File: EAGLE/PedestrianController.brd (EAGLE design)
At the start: 30 x 80 mm, 16 parts, among them CON1 FTDI, CON2 DS3231, CON3 AC110V, CON4 SIGNAL, IC1 ESP-WROOM-02

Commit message: Rearranged.
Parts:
- moved PROGSW 53.0 mm to (8.71, 79.7)
- moved R4 38.1 mm to (43.7, 53.8)
- moved RSTSW 36.0 mm to (8.71, 71.6)
- moved R5 35.0 mm to (43.7, 62.9)
- moved R6 35.0 mm to (43.7, 59.9)
- moved R7 35.0 mm to (43.7, 56.9)
- moved R1 27.8 mm to (43.7, 78.0)
- moved R2 27.8 mm to (43.7, 75.0)
- moved R3 27.8 mm to (43.7, 72.0)
- moved CON2 21.4 mm to (41.4, 46.1)
- moved CON1 14.0 mm to (8.55, 58.5), turned to 90 degrees
- moved SSR1 13.3 mm to (4.97, 27.3)
- moved CON4 11.7 mm to (34.8, 7.94)
- moved IC1 11.7 mm to (26.2, 77.7)
- moved SSR2 11.4 mm to (15.0, 27.3)
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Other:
- board size 30 x 80 mm -> 57.8 x 85 mm
- board text added: "Pedestrian Controller"
- board text added: "TAKACHI SW-100"
- board text added: "https://github.com/kekyo/PedestrianController"

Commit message: Rearranged parts.
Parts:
- moved R4 23.0 mm to (43.7, 76.8)
- moved R1 21.0 mm to (43.7, 57.0)
- moved R2 15.0 mm to (43.7, 60.0)
- moved R5 11.0 mm to (43.7, 73.9)
- moved R6 11.0 mm to (43.7, 70.9)
- moved R7 6.00 mm to (43.7, 62.9)
- moved R3 4.00 mm to (43.7, 68.0)
- moved CON3 2.00 mm to (13.8, 7.94)
- moved PROGSW 2.00 mm to (8.71, 77.7)
- moved RSTSW 2.00 mm to (8.71, 69.6)
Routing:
- net GND: track 0.00 -> 113.7 mm, vias 0 -> 1
- net +3V3: track 0.00 -> 101.6 mm
- net N$2: track 0.00 -> 58.6 mm, vias 0 -> 1
- net N$9: track 0.00 -> 58.4 mm
- net N$3: track 0.00 -> 51.9 mm
- net N$10: track 0.00 -> 50.1 mm
- net N$1: track 0.00 -> 45.9 mm
- net N$4: track 0.00 -> 41.5 mm
- net N$15: track 0.00 -> 35.3 mm, vias 0 -> 1
- net RXD: track 0.00 -> 35.3 mm
- net SCL: track 0.00 -> 33.7 mm
- net TXD: track 0.00 -> 32.4 mm
- net AC110V: track 0.00 -> 28.1 mm
- net WALK: track 0.00 -> 27.0 mm
- net SDA: track 0.00 -> 26.6 mm
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
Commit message: Rerouted with broad rule.
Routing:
- net N$14: track 23.8 -> 36.2 mm
- net N$13: track 25.6 -> 31.1 mm
- net RXD: track 35.3 -> 30.7 mm, vias 0 -> 1
- net GND: track 113.7 -> 117.7 mm, vias 1 -> 0
- net N$1: track 45.9 -> 42.9 mm, vias 0 -> 1
- net N$9: track 58.4 -> 56.5 mm
- net N$10: track 50.1 -> 52.0 mm
- net N$2: track 58.6 -> 60.3 mm
- net N$4: track 41.5 -> 42.7 mm
- net +3V3: track 101.6 -> 101.3 mm, vias 0 -> 1

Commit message: Rerouted with broad rule.
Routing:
- net +3V3: track 101.3 -> 130.3 mm, vias 1 -> 0
- net N$14: track 36.2 -> 23.8 mm
- net SDA: track 26.6 -> 34.4 mm, vias 0 -> 1
- net SCL: track 33.9 -> 39.9 mm, vias 0 -> 1
- net TXD: track 32.3 -> 37.1 mm
- net GND: track 117.7 -> 122.2 mm
- net N$3: track 52.0 -> 55.8 mm
- net N$15: track 35.3 -> 38.7 mm
- net N$10: track 52.0 -> 48.6 mm
- net N$1: track 42.9 -> 46.2 mm, vias 1 -> 0
- net N$9: track 56.5 -> 58.8 mm, vias 0 -> 1
- net N$2: track 60.3 -> 62.5 mm
- net RXD: vias 1 -> 0

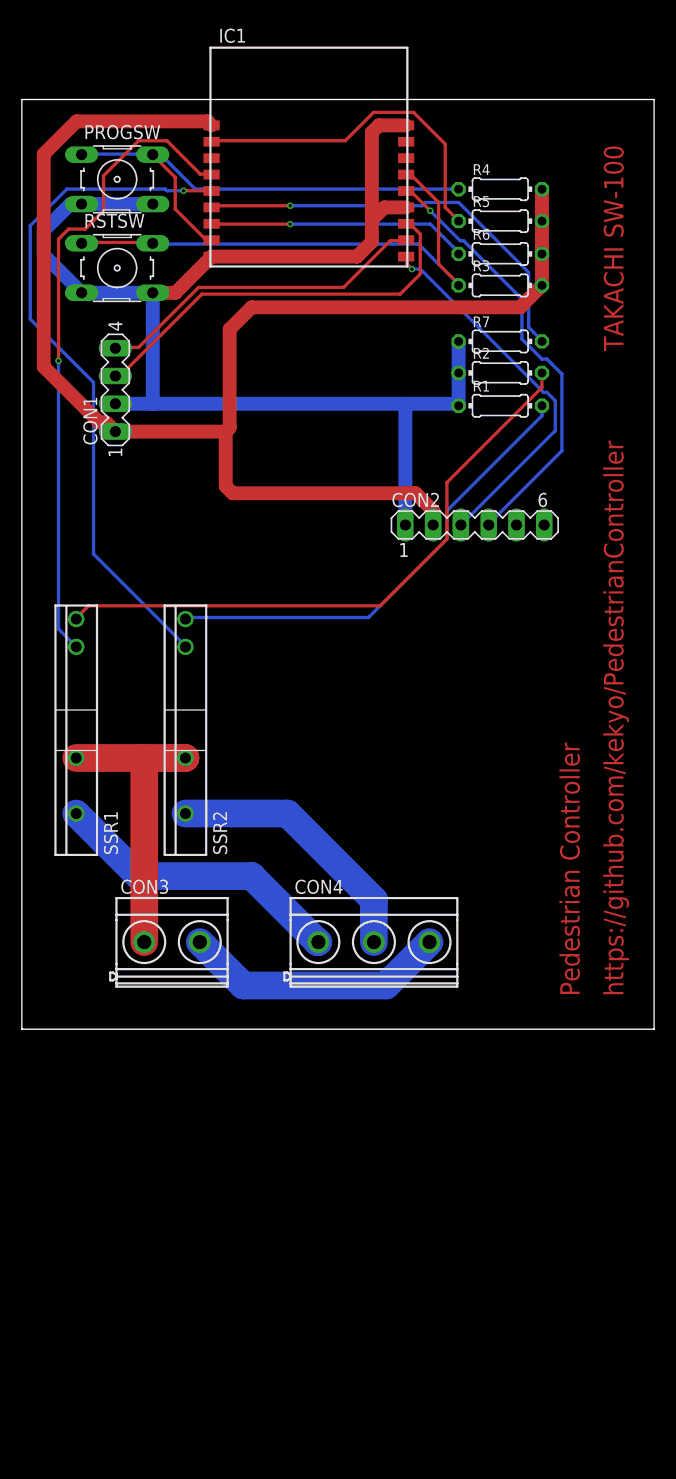
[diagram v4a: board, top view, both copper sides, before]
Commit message: Rearrange parts, add leds.
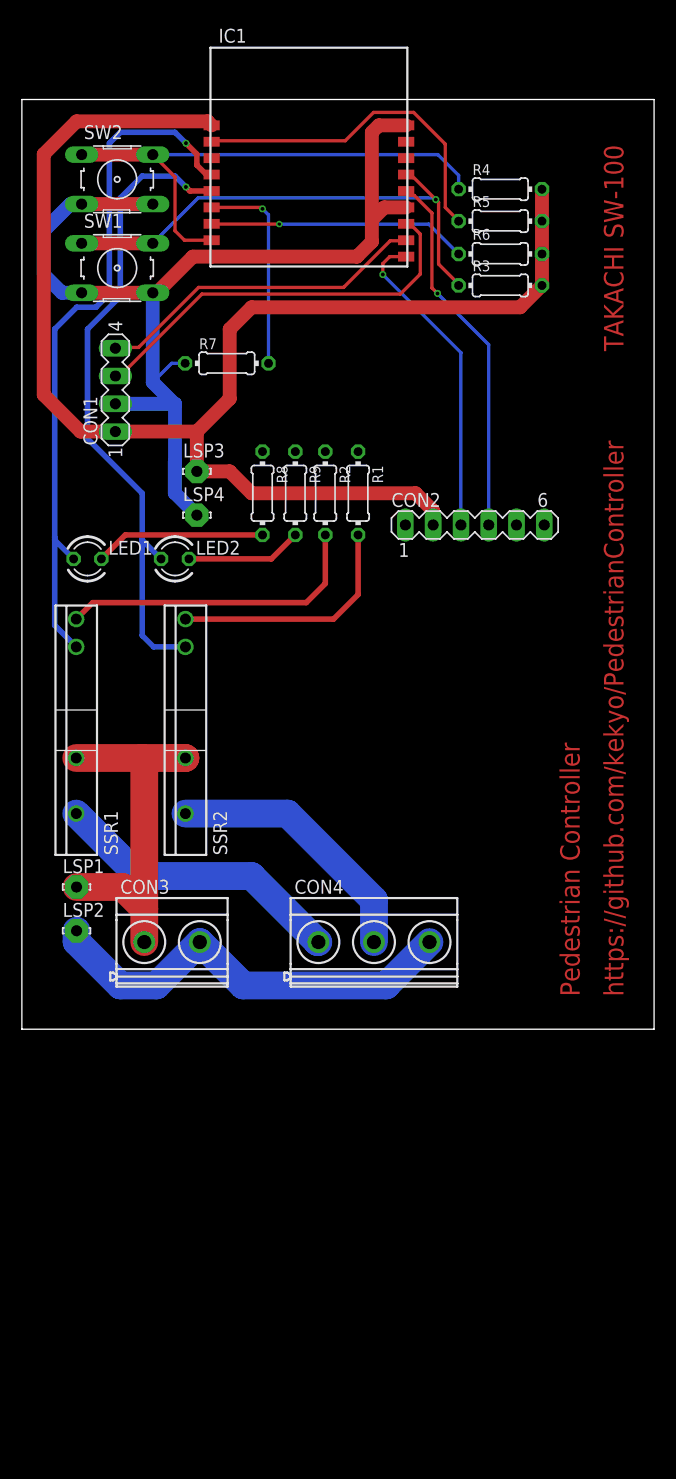
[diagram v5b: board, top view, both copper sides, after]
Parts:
- added LED1, LED2: TLLR4400, PedestrianController:LED3MM
- added LSP1, LSP2, LSP3, LSP4: LSP10, PedestrianController:LSP10
- added R8, R9: 200, PedestrianController:0204/7
- R1, R2: value 10K -> 100
- SW1: value (none) -> RSTSW
- SW2: value (none) -> PROGSW
- moved R7 25.1 mm to (18.7, 60.9)
- moved R2 19.4 mm to (27.7, 49.0), turned to 270 degrees
- moved R1 15.3 mm to (30.7, 49.0), turned to 270 degrees
- renumbered PROGSW to SW2, RSTSW to SW1
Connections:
- new net N$5: LED1.K, R8.2
- new net N$6: LED2.K, R9.2
- net +3V3: now also LSP3.MP
- net AC110V: now also LSP1.MP
- net ACCOM: now also LSP2.MP
- net GND: now also LSP4.MP, R8.1, R9.1
- net N$2: now also LED2.A
- net N$9: now also LED1.A
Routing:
- net N$3: track 55.8 -> 28.6 mm
- net GND: track 122.2 -> 95.7 mm
- net N$4: track 42.7 -> 22.2 mm
- net N$15: track 38.7 -> 19.1 mm
- net N$5: track 0.00 -> 15.6 mm
- net ACCOM: track 24.3 -> 39.9 mm
- net N$6: track 0.00 -> 10.6 mm
- net AC110V: track 28.1 -> 35.1 mm
- net SCL: track 39.9 -> 33.9 mm
- net N$9: track 58.8 -> 64.4 mm
- net SDA: track 34.4 -> 29.3 mm
- net N$2: track 62.5 -> 60.0 mm
- net N$1: track 46.2 -> 48.6 mm
- net N$10: track 48.6 -> 46.5 mm, vias 0 -> 1
- net +3V3: track 130.3 -> 132.1 mm

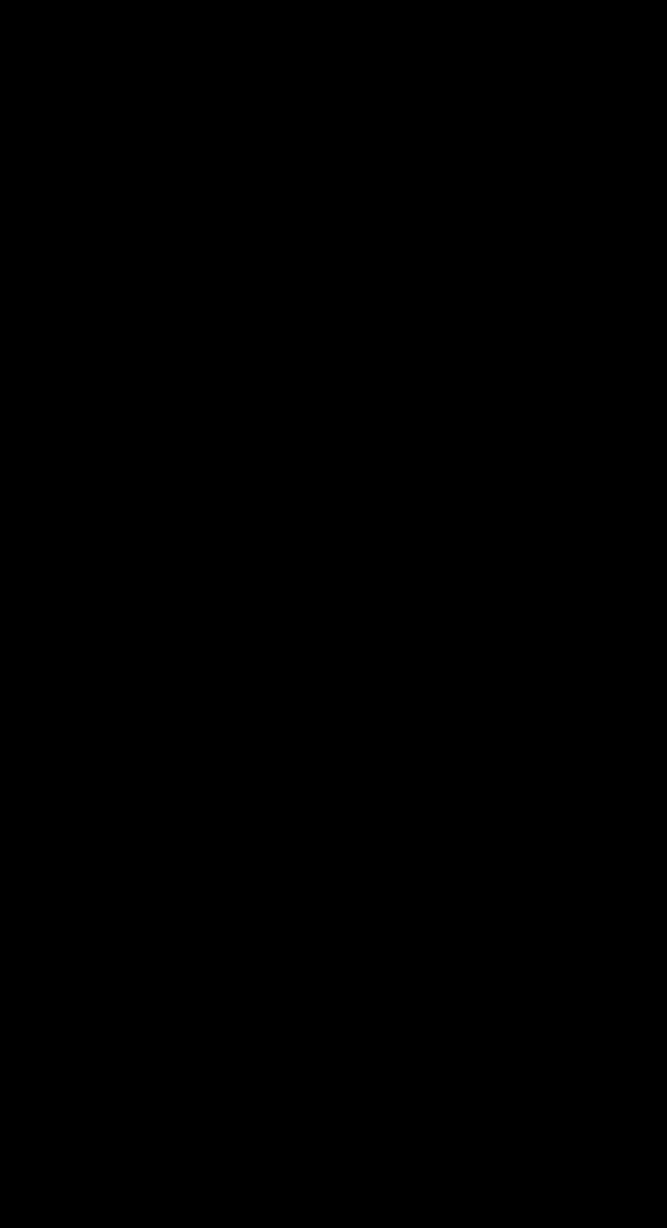
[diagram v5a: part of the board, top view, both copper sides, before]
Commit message: Add status LEDs.
* Improvement
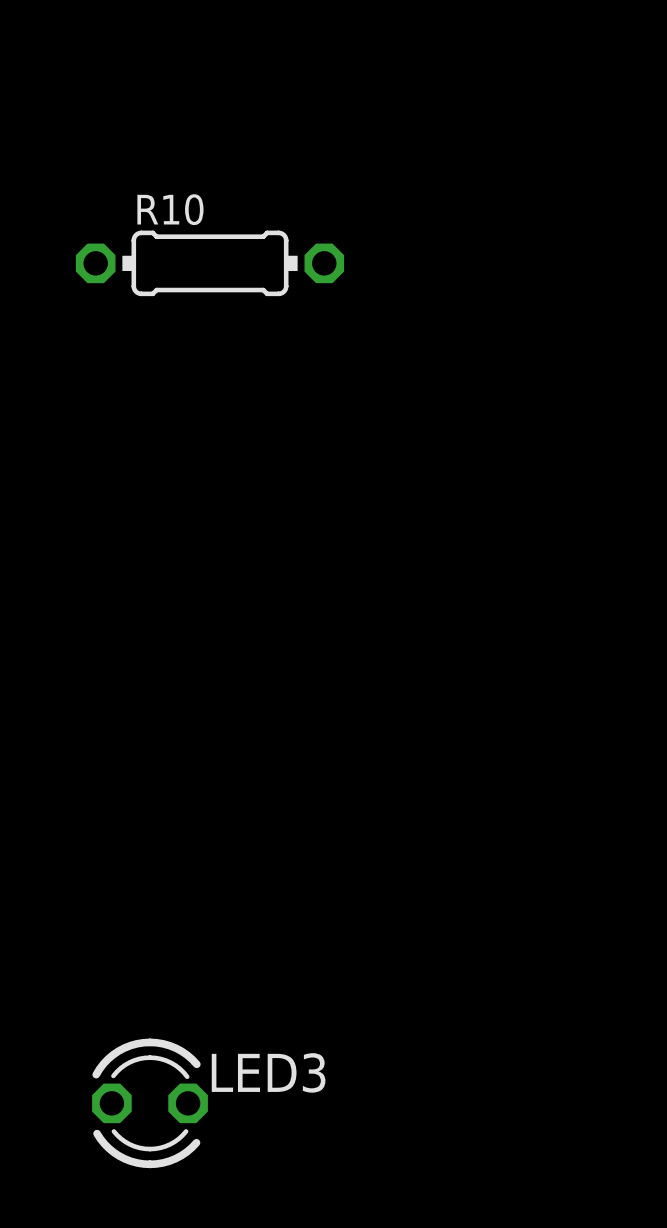
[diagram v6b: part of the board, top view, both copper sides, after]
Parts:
- added LED3: (no value), PedestrianController:LED3MM
- added R10: 200, PedestrianController:0204/7
- LED1, LED2: value TLLR4400 -> (none)
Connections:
- new net N$11: LED3.K, R10.2
- new net N$8: IC1.3, LED3.A
- net GND: now also R10.1
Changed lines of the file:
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@@
 <element name="R8" library="PedestrianController" package="0204/7" package3d_urn="urn:adsk.eagle:package:25945/1" value="200" x="22" y="49" rot="R270"/>
 <element name="R9" library="PedestrianController" package="0204/7" package3d_urn="urn:adsk.eagle:package:25945/1" value="200" x="25" y="49" rot="R270"/>
-<element name="LED1" library="PedestrianController" package="LED3MM" package3d_urn="urn:adsk.eagle:package:15797/1" value="TLLR4400" x="6" y="43">
+<element name="LED1" library="PedestrianController" package="LED3MM" package3d_urn="urn:adsk.eagle:package:15797/1" value="" x="6" y="43">
 <attribute name="MF" value="VISHAY SEMICONDUCTOR" x="6" y="43" size="1.778" layer="27" display="off"/>
 <attribute name="OC_FARNELL" value="1612437" x="6" y="43" size="1.778" layer="27" display="off"/>
 </element>
-<element name="LED2" library="PedestrianController" package="LED3MM" package3d_urn="urn:adsk.eagle:package:15797/1" value="TLLR4400" x="14" y="43">
+<element name="LED2" library="PedestrianController" package="LED3MM" package3d_urn="urn:adsk.eagle:package:15797/1" value="" x="14" y="43">
 <attribute name="MF" value="VISHAY SEMICONDUCTOR" x="14" y="43" size="1.778" layer="27" display="off"/>
 <attribute name="OC_FARNELL" value="1612437" x="14" y="43" size="1.778" layer="27" display="off"/>
+</element>
+<element name="R10" library="PedestrianController" package="0204/7" package3d_urn="urn:adsk.eagle:package:25945/1" value="200" x="5" y="-9"/>
+<element name="LED3" library="PedestrianController" package="LED3MM" package3d_urn="urn:adsk.eagle:package:15797/1" value="" x="3" y="-37">
+<attribute name="MF" value="VISHAY SEMICONDUCTOR" x="3" y="-37" size="1.778" layer="27" display="off"/>
+<attribute name="OC_FARNELL" value="1612437" x="3" y="-37" size="1.778" layer="27" display="off"/>
 </element>
 </elements>
@@
 <contactref element="R9" pad="1"/>
 <contactref element="R8" pad="1"/>
+<contactref element="R10" pad="1"/>
+<wire x1="27.74" y1="52.81" x2="30.74" y2="52.81" width="0" layer="19" extent="1-1"/>
+<wire x1="25" y1="52.81" x2="27.74" y2="52.81" width="0" layer="19" extent="1-1"/>
 <wire x1="22" y1="52.81" x2="25" y2="52.81" width="0" layer="19" extent="1-1"/>
-<wire x1="30.74" y1="52.81" x2="22" y2="52.81" width="0" layer="19" extent="1-1"/>
-<wire x1="27.74" y1="52.81" x2="30.74" y2="52.81" width="0" layer="19" extent="1-1"/>
-<wire x1="14" y1="51.855725" x2="27.74" y2="52.81" width="0" layer="19" extent="16-16"/>
-<wire x1="35.06" y1="46.1" x2="25" y2="52.81" width="0" layer="19" extent="1-1"/>
+<wire x1="35.06" y1="46.1" x2="30.74" y2="52.81" width="0" layer="19" extent="1-1"/>
+<wire x1="14" y1="51.855725" x2="22" y2="52.81" width="0" layer="19" extent="16-16"/>
+<wire x1="1.19" y1="-9" x2="16" y2="47" width="0" layer="19" extent="1-1"/>
 </signal>
 <signal name="ACCOM" class="1">
@@
 <wire x1="22.81" y1="43" x2="15.27" y2="43" width="0.508" layer="1"/>
 </signal>
+<signal name="N$11">
+<contactref element="R10" pad="2"/>
+<contactref element="LED3" pad="K"/>
+<wire x1="8.81" y1="-9" x2="4.27" y2="-37" width="0" layer="19" extent="1-1"/>
+</signal>
+<signal name="N$8">
+<contactref element="IC1" pad="3"/>
+<contactref element="LED3" pad="A"/>
+<wire x1="1.73" y1="-37" x2="17.3475" y2="79.635" width="0" layer="19" extent="1-1"/>
+</signal>
 </signals>

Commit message: Rearrange wires.
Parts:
- added C1: 100u, PedestrianController:C050-024X044
- added C2: 0.1u, PedestrianController:C050-024X044
- R10, R8, R9: value 200 -> 510
- moved LED3 96.1 mm to (23.0, 57.0)
- moved R10 70.8 mm to (30.7, 57.0), turned to 180 degrees
- moved R7 12.0 mm to (30.7, 60.9), turned to 180 degrees
- moved CON2 2.00 mm to (41.4, 48.1)
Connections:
- net +3V3: now also C1.1, C2.1
- net GND: now also C1.2, C2.2
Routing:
- net GND: track 95.7 -> 137.1 mm
- net N$8: track 0.00 -> 25.6 mm, vias 0 -> 1
- net N$2: track 60.0 -> 66.9 mm
- net +3V3: track 132.1 -> 126.4 mm
- net N$15: track 19.1 -> 22.5 mm
- net N$11: track 0.00 -> 2.66 mm
- net N$10: track 46.5 -> 49.0 mm
- net SDA: track 29.3 -> 27.3 mm
- net SCL: track 33.9 -> 31.9 mm
- net N$9: track 64.4 -> 66.2 mm
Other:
- board text added: "SW-100"
- board text removed: "TAKACHI SW-100"
